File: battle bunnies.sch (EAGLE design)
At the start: 59 parts, among them IC1 CP2104, Q1 mmbt2222, Q2 mmbt2222, SW2 KMR2, U1 PCA9685, U2 SPX3819, U3 MCP73831T-2ACI/OT, X2 ESP-12, X4 20329

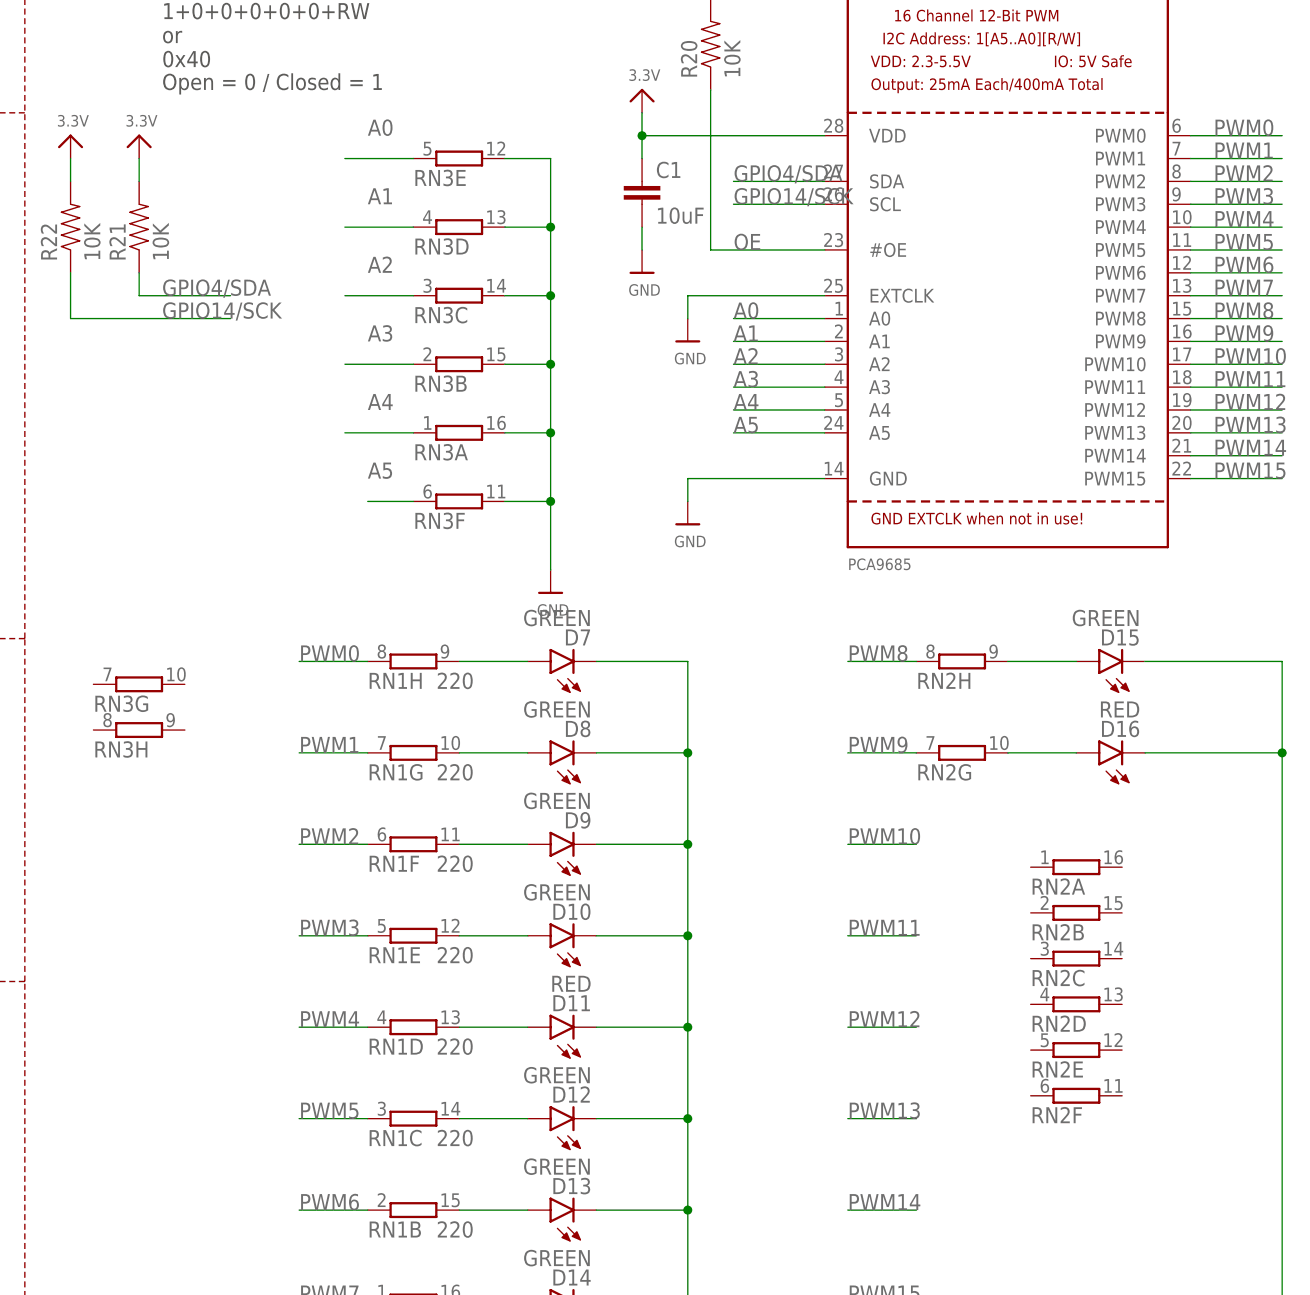
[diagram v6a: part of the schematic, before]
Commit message: more silk changes
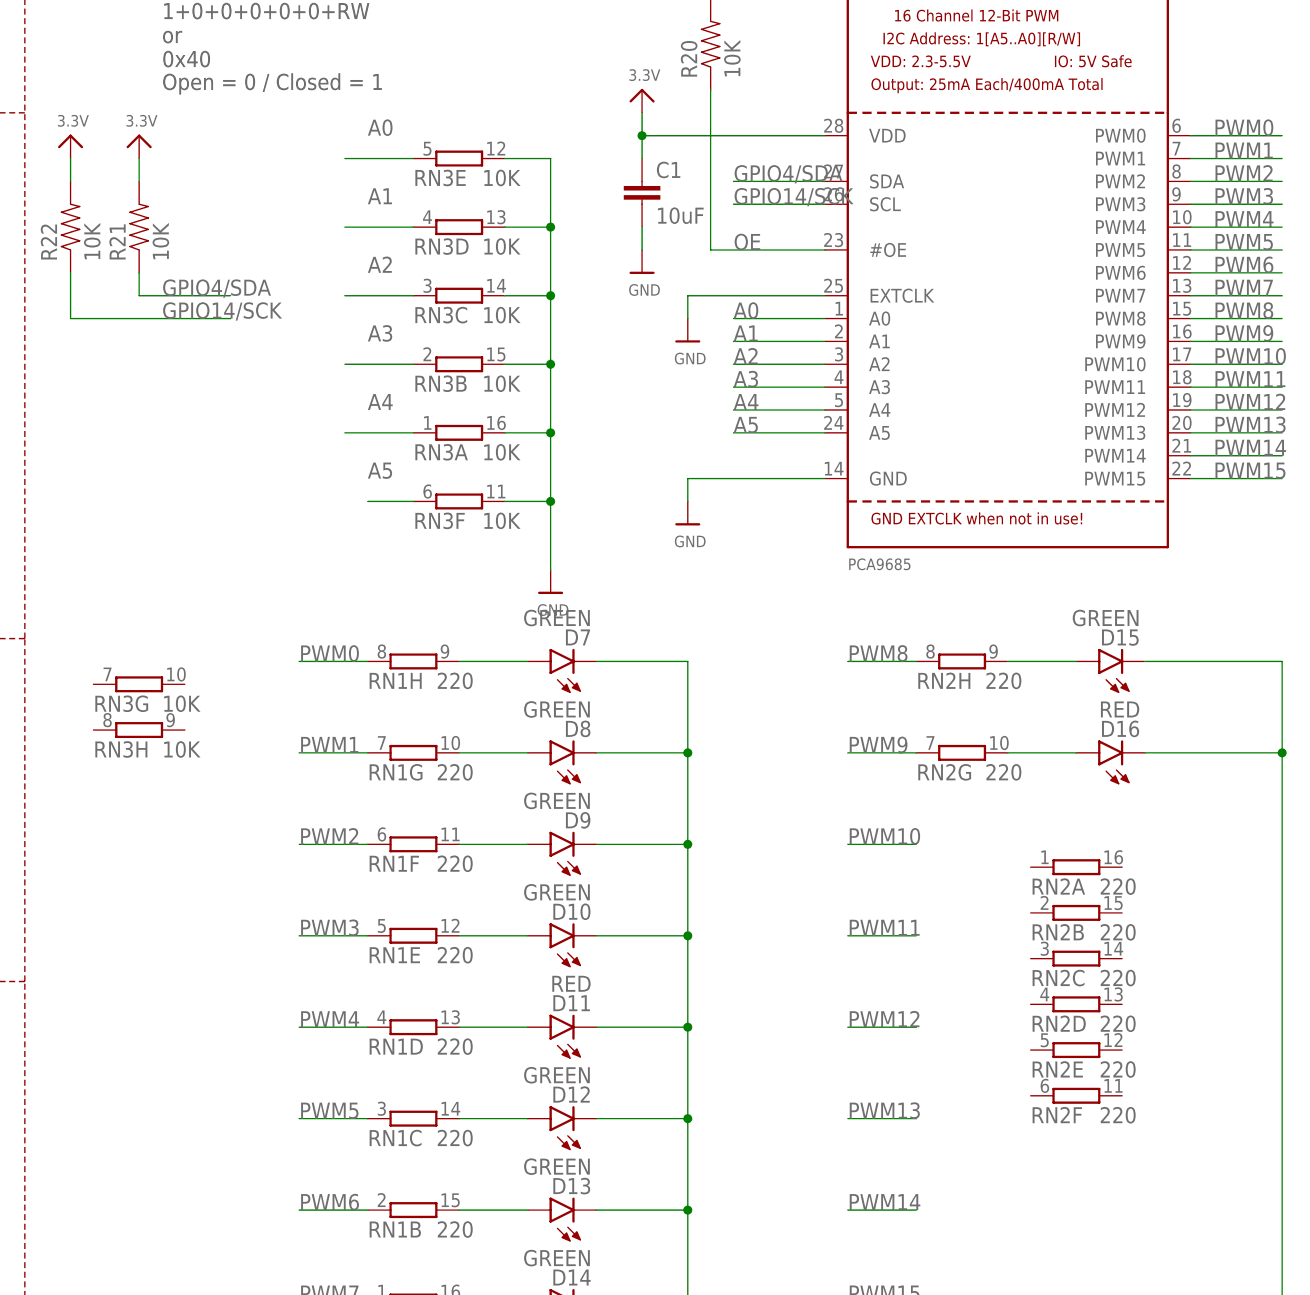
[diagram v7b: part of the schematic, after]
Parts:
- RN2: value (none) -> 220
- RN3: value (none) -> 10K
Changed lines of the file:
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@@
 <part name="GND7" library="supply1" deviceset="GND" device=""/>
 <part name="RN1" library="resistor-dil" deviceset="8R-N" device="EXB2HV" value="220"/>
-<part name="RN2" library="resistor-dil" deviceset="8R-N" device="EXB2HV"/>
-<part name="RN3" library="resistor-dil" deviceset="8R-N" device="EXB2HV"/>
+<part name="RN2" library="resistor-dil" deviceset="8R-N" device="EXB2HV" value="220"/>
+<part name="RN3" library="resistor-dil" deviceset="8R-N" device="EXB2HV" value="10K"/>
 </parts>
 <sheets>

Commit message: Initial sensor board work
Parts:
- removed D10, D12, D13, D14, D15, D7, D8, D9: GREEN, SparkFun-LED:LED-GREEN0603
- removed D11, D16: RED, SparkFun-LED:LED-RED0603
- removed D6: (no value), SparkFun-LED:LTE-302
- removed IRRX: TSOP38, Opto-electronics:TSOP38
- removed JP4: (no value), pinhead:PINHD-1X15
- removed R20, R21, R22: 10K, SparkFun-Passives:RESISTOR0805-RES
- removed R23: 270, microbuilder:RESISTOR_0603_NOOUT
- removed RN1, RN2: 220, resistor-dil:8R-NEXB2HV
- removed RN3: 10K, resistor-dil:8R-NEXB2HV
- added C2: 0.1uF, SparkFun-Capacitors:0.1UF-25V-5%(0603)
- added R11, R13, R14, R17: 4.7K, SparkFun-Resistors:4.7KOHM-1/10W-1%(0603)
- added SJ4: EN ADR PULLUP, SparkFun-Passives:JUMPER-PAD-3-2OF3_NC_BY_TRACE_SMALL
- C1: value 10uF -> 0.1uF; device SparkFun-Capacitors:10UF10V10%(0805) -> SparkFun-Capacitors:0.1UF-25V-5%(0603)
- JP2: device pinhead:PINHD-1X15 -> pinhead:PINHD-1X22
- U$31: value AA1 -> 18650; device Electromechanical:AA1 -> Warthog9-Batteries:18650
- U1: value PCA9685 -> BME280; device microbuilder:PCA9685 -> BME280ComponentLibrary:BME280
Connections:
- removed net A0: RN3E.1, U1.A0
- removed net A1: RN3D.1, U1.A1
- removed net A2: RN3C.1, U1.A2
- removed net A3: RN3B.1, U1.A3
- removed net A4: RN3A.1, U1.A4
- removed net A5: RN3F.1, U1.A5
- removed net N$14: D6.A, R23.1
- removed net N$16: D14.A, RN1A.2
- removed net N$17: D12.A, RN1C.2
- removed net N$18: D11.A, RN1D.2
- removed net N$19: D10.A, RN1E.2
- removed net N$20: D9.A, RN1F.2
- removed net N$21: D8.A, RN1G.2
- removed net N$22: D7.A, RN1H.2
- removed net N$23: D15.A, RN2H.2
- removed net N$24: D16.A, RN2G.2
- removed net OE: R20.1, U1.#OE
- removed net PWM0: RN1H.1, U1.PWM0
- removed net PWM1: RN1G.1, U1.PWM1
- removed net PWM10: JP2.13, U1.PWM10
- removed net PWM11: JP2.14, U1.PWM11
- removed net PWM12: JP2.15, U1.PWM12
- removed net PWM13: JP4.13, U1.PWM13
- removed net PWM14: JP4.14, U1.PWM14
- removed net PWM15: JP4.15, U1.PWM15
- removed net PWM2: RN1F.1, U1.PWM2
- removed net PWM3: RN1E.1, U1.PWM3
- removed net PWM4: RN1D.1, U1.PWM4
- removed net PWM5: RN1C.1, U1.PWM5
- removed net PWM6: RN1B.1, U1.PWM6
- removed net PWM7: RN1A.1, U1.PWM7
- removed net PWM8: RN2H.1, U1.PWM8
- removed net PWM9: RN2G.1, U1.PWM9
- new net !CS: R14.1, U1.!CS
- new net CLK: JP2.12, X2.CLK
- new net CS: JP2.15, X2.CS
- new net DI: JP2.11, X2.DI
- new net DO: JP2.14, X2.DO
- new net GPIO10: JP2.13, X2.GPIO10
- new net GPIO9: JP2.10, X2.GPIO9
- new net SDO/ADR: SJ4.2, U1.SDO/ADR
- net 3.3V: now also C2.1, R11.2, R13.2, R14.2, R17.2, U1.VDDIO; no longer IRRX.VS, JP4.1, R21.2, R22.2, R23.2
- net ADC: now also JP2.21; no longer JP4.5
- net CH_PD: now also JP2.20; no longer JP4.10
- net GND: now also C2.2, SJ4.1, U1.GND1, U1.GND2; no longer D10.C, D11.C, D12.C, D13.C, D14.C, D15.C, D16.C, D7.C, D8.C, D9.C, IRRX.GND, JP4.2, R20.2, RN3A.2, RN3B.2, RN3C.2, RN3D.2, RN3E.2, RN3F.2, U1.EXTCLK, U1.GND
- net GPIO0: now also JP2.7; no longer JP2.3
- net GPIO12/MISO: now also JP2.17, R11.1, U1.SDI/SDA; no longer D6.C, JP2.12
- net GPIO13/MOSI: now also JP2.16; no longer JP2.6
- net GPIO14/SCK: now also JP2.18, R13.1, U1.SCK/SCL; no longer JP4.6, R22.1, U1.SCL
- net GPIO15: now also JP2.9; no longer JP2.7
- net GPIO16: now also JP2.19; no longer JP2.9
- net GPIO2: now also JP2.8; no longer JP2.4
- net GPIO4/SDA: now also JP2.6; no longer JP4.7, R21.1, U1.SDA
- net GPIO5/SCL: now also JP2.5; no longer IRRX.OUT, JP2.11
- net N$15: now also R17.1, SJ4.3; no longer D13.A, RN1B.2
- net RESET: now also JP2.22; no longer JP2.5
- net RXD: now also JP2.4; no longer JP4.8
- net TXD: now also JP2.3; no longer JP4.9
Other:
- note added: "BME280"
- note added: "SJ4 controls the lowest bit of the I2C address--can be: 0x1110110 0x1110111 Open for SPI 3-wire mode"
- note removed: "1 + A5 + A4 + A3 + A2 + A1 +A1 + RW = 1+0+0+0+0+0+RW or 0x40"
- note removed: "I2C Address ="
- note removed: "Infrared (IR) stuff"
- note removed: "Note: I2C, on the ESP8266, is done via software and usable from *ANY* pins So ignore the hardware pins, and move on https://docs.micropython.org/en/latest/esp8266/esp8266/quickref.html#i2c-bus"
- note removed: "Open = 0 / Closed = 1"
- note removed: "TSOP38238"
- moved on the sheet: C1, S2, S3
